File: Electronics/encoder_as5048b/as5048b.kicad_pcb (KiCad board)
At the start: 2 copper layers, 31 x 28 mm, 16 parts, among them IC1 AS5048B-HTSP, J1 Conn_01x04_Male, J2 Conn_01x04_Male

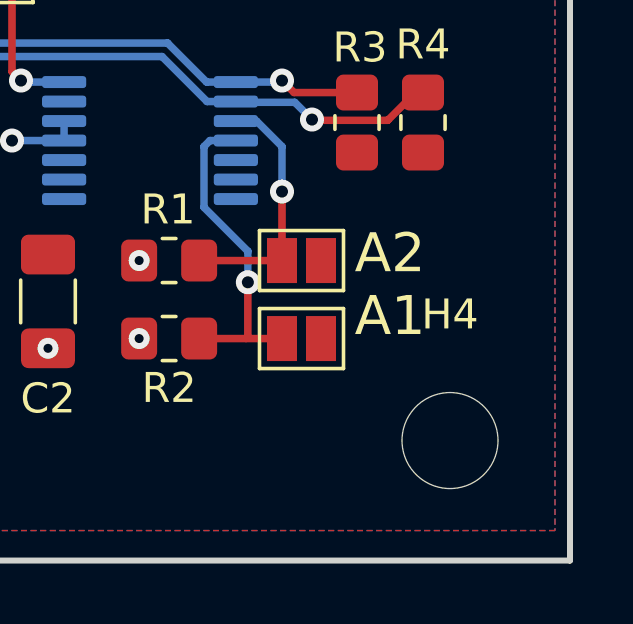
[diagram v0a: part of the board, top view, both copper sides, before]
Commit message: Update encoder PCB. Add driver for INA226 power monitor chip.
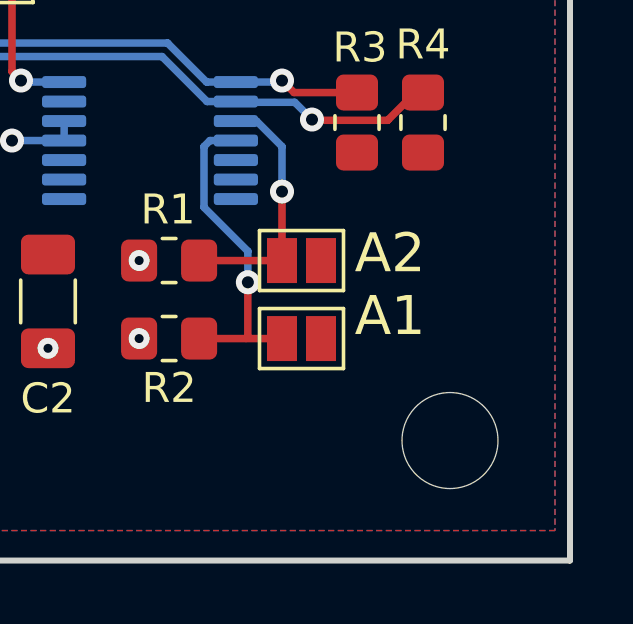
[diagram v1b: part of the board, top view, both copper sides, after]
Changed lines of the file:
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@@
     (clearance 1)
     (attr exclude_from_pos_files)
-    (fp_text reference "H4" (at 0 -4.2) (layer "F.SilkS")
+    (fp_text reference "H4" (at 0 -4.2) (layer "F.SilkS") hide
         (effects (font (size 1 1) (thickness 0.15)))
     )
